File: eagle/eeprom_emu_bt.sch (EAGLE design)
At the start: 9 parts

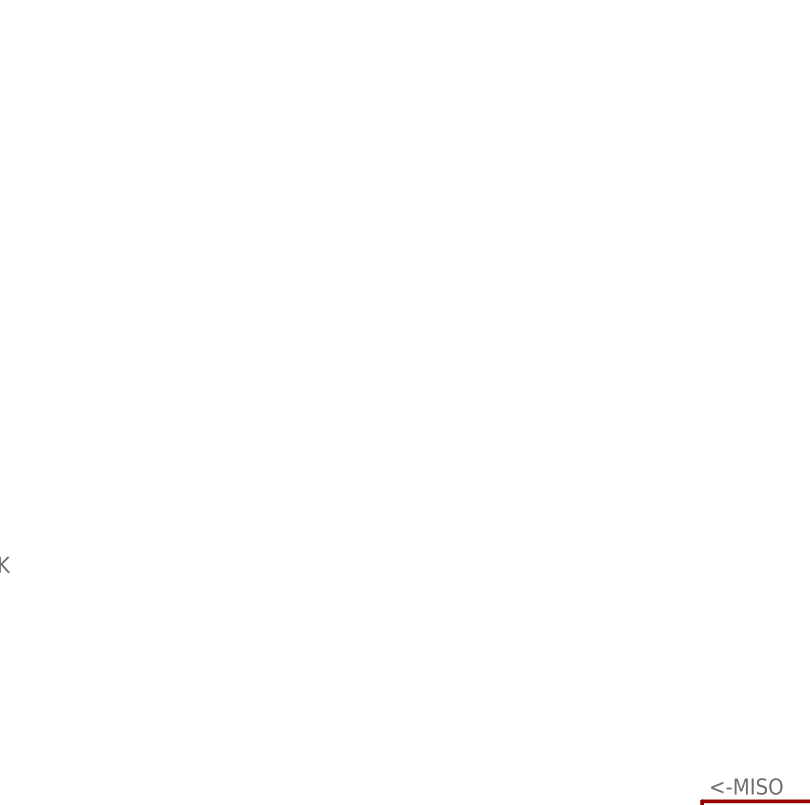
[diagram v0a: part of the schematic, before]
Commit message: 27c256 added
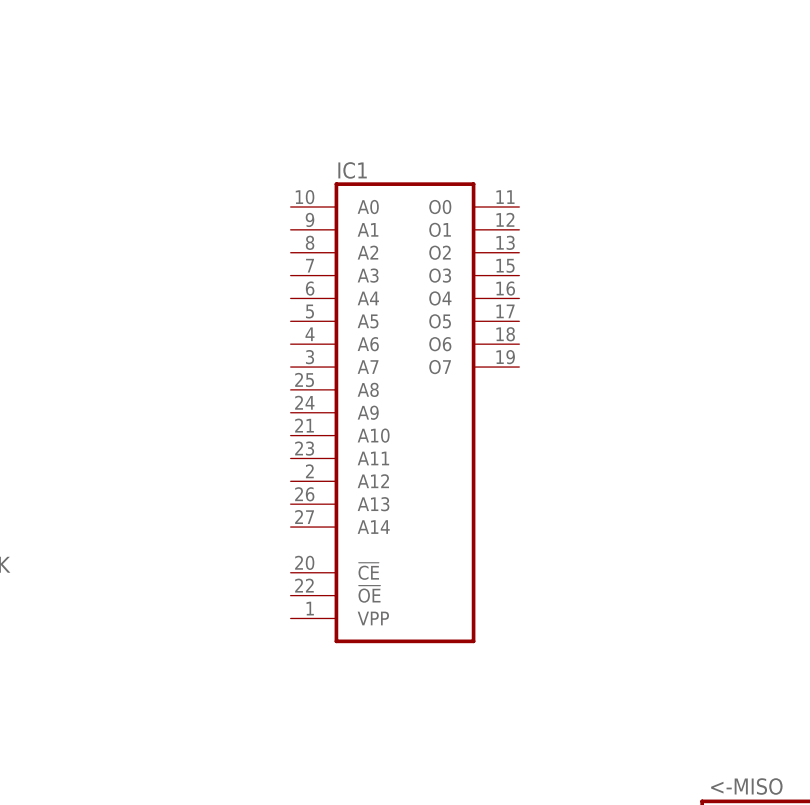
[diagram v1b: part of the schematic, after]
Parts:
- added IC1: (no value), memory:27256
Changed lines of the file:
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@@
 <part name="MAINGND18" library="supply2" deviceset="GND" device=""/>
 <part name="Y1" library="SparkFun-FreqCtrl" deviceset="CRYSTAL" device="HC49US"/>
+<part name="IC1" library="memory" deviceset="27256" device=""/>
 </parts>
 <sheets>
@@
 <instance part="MAINGND18" gate="GND" x="132.08" y="137.16"/>
 <instance part="Y1" gate="G$1" x="162.56" y="172.72" rot="R90"/>
+<instance part="IC1" gate="A" x="276.86" y="160.02"/>
 </instances>
 <busses>

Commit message: eagles
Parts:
- added BLUETOOTH: (no value), SparkFun-Connectors:M05PTH
- added IC2: IS62C256AL-45U, memory-issi-asynsram:IS62C256AL-45U
- added IC3, IC4, IC5, IC6, IC7, IC8: 74HCT541DW, 74xx-eu:74HCT541DW
- added IC9: 74HC573D, 74xx-eu:74HC573D
- added U1: SST39SF040-70-4I-NHE, Silicon_Storage_Tech_By_element14_Batch_1:SST39SF040-70-4I-NHE
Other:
- moved on the sheet: IC1
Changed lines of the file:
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@@
 <part name="Y1" library="SparkFun-FreqCtrl" deviceset="CRYSTAL" device="HC49US"/>
 <part name="IC1" library="memory" deviceset="27256" device=""/>
+<part name="U1" library="Silicon_Storage_Tech_By_element14_Batch_1" deviceset="SST39SF040-70-4I-NHE" device=""/>
+<part name="IC2" library="memory-issi-asynsram" deviceset="IS62C256AL-*" device="U" technology="45"/>
+<part name="IC3" library="74xx-eu" deviceset="74*541" device="DW" technology="HCT"/>
+<part name="IC4" library="74xx-eu" deviceset="74*541" device="DW" technology="HCT"/>
+<part name="IC5" library="74xx-eu" deviceset="74*541" device="DW" technology="HCT"/>
+<part name="IC6" library="74xx-eu" deviceset="74*541" device="DW" technology="HCT"/>
+<part name="IC7" library="74xx-eu" deviceset="74*541" device="DW" technology="HCT"/>
+<part name="IC8" library="74xx-eu" deviceset="74*541" device="DW" technology="HCT"/>
+<part name="IC9" library="74xx-eu" deviceset="74*573" device="D" technology="HC"/>
+<part name="BLUETOOTH" library="SparkFun-Connectors" deviceset="M05" device="PTH"/>
 </parts>
 <sheets>
@@
 <instance part="MAINGND18" gate="GND" x="132.08" y="137.16"/>
 <instance part="Y1" gate="G$1" x="162.56" y="172.72" rot="R90"/>
-<instance part="IC1" gate="A" x="276.86" y="160.02"/>
+<instance part="IC1" gate="A" x="307.34" y="172.72"/>
+<instance part="U1" gate="A" x="304.8" y="50.8"/>
+<instance part="IC2" gate="SRAM" x="360.68" y="175.26"/>
+<instance part="IC3" gate="A" x="419.1" y="210.82"/>
+<instance part="IC4" gate="A" x="419.1" y="170.18"/>
+<instance part="IC5" gate="A" x="419.1" y="129.54"/>
+<instance part="IC6" gate="A" x="419.1" y="78.74"/>
+<instance part="IC7" gate="A" x="419.1" y="38.1"/>
+<instance part="IC8" gate="A" x="419.1" y="0"/>
+<instance part="IC9" gate="A" x="360.68" y="124.46"/>
+<instance part="BLUETOOTH" gate="G$1" x="119.38" y="101.6"/>
 </instances>
 <busses>

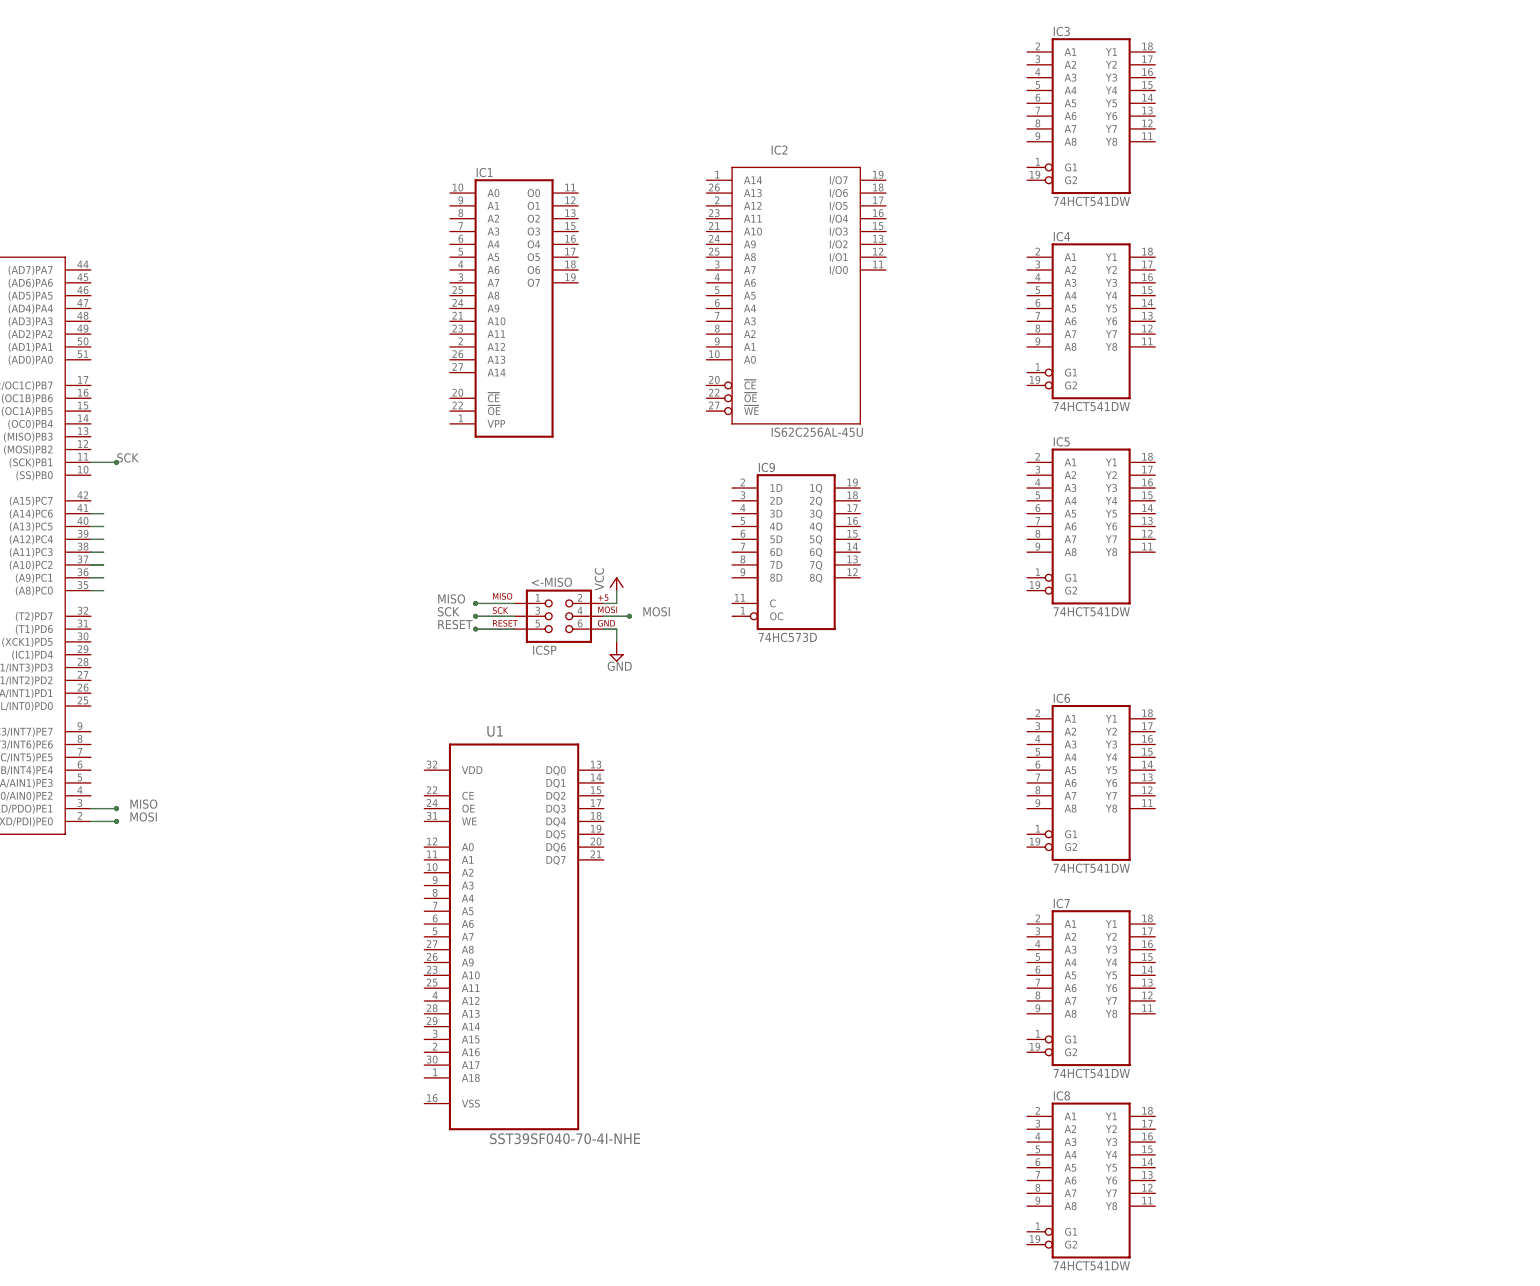
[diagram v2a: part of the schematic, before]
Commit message: or gate added for CE of sram
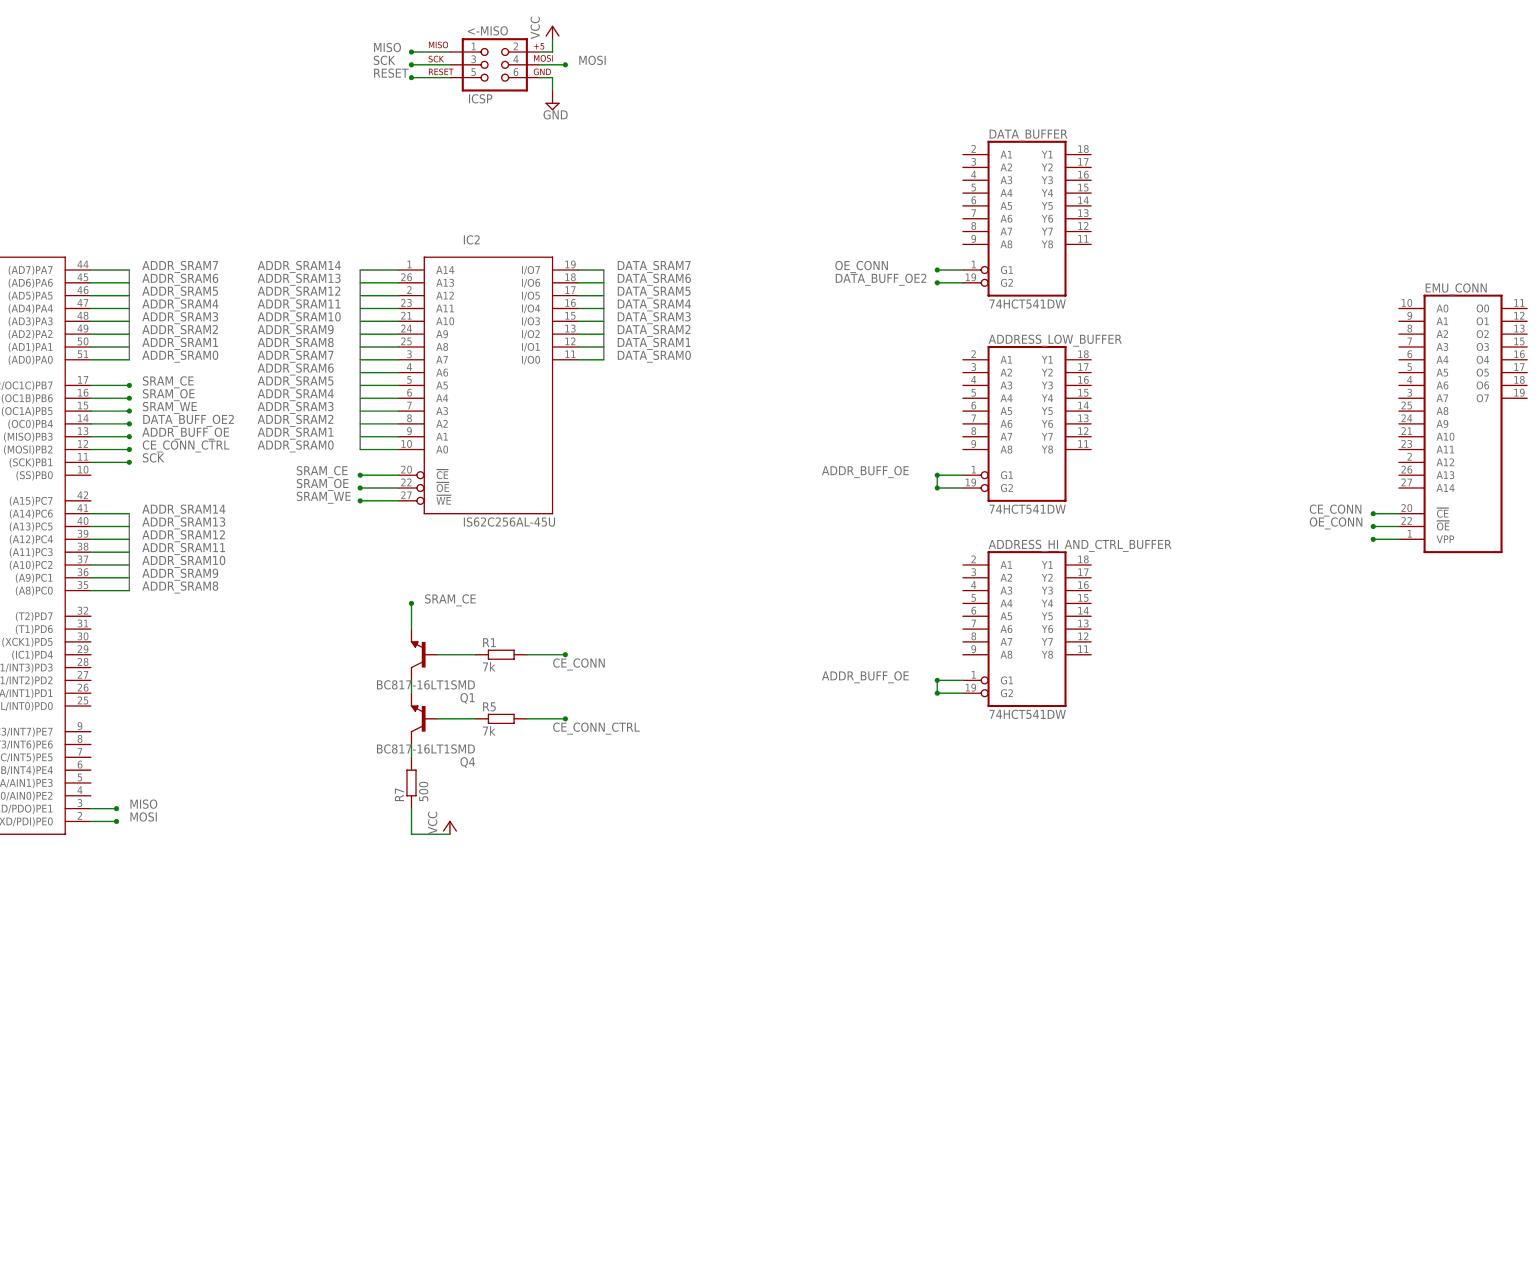
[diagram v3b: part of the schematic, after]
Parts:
- removed IC1: (no value), memory:27256
- removed IC3, IC4, IC5, IC6, IC7, IC8: 74HCT541DW, 74xx-eu:74HCT541DW
- removed IC9: 74HC573D, 74xx-eu:74HC573D
- removed U1: SST39SF040-70-4I-NHE, Silicon_Storage_Tech_By_element14_Batch_1:SST39SF040-70-4I-NHE
- added ADDRESS_HI_AND_CTRL_BUFFER, ADDRESS_LOW_BUFFER, DATA_BUFFER: 74HCT541DW, 74xx-eu:74HCT541DW
- added EMU_CONN: (no value), memory:27256
- added Q1, Q4: BC817-16LT1SMD, transistor-npn:BC817-16LT1SMD
- added R1, R5: 7k, rcl:R-EU_R0805
- added R7: 500, rcl:R-EU_R0805
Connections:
- removed net A10: ..(A10)PC2
- removed net A11: ..(A11)PC3
- removed net A12: ..(A12)PC4
- removed net A13: ..(A13)PC5
- removed net A14: ..(A14)PC6
- removed net A8: ..(A8)PC0
- removed net A9: ..(A9)PC1
- new net ADDR_BUFF_OE: ..(MISO)PB3, ADDRESS_HI_AND_CTRL_BUFFERA.G1, ADDRESS_HI_AND_CTRL_BUFFERA.G2, ADDRESS_LOW_BUFFERA.G1, ADDRESS_LOW_BUFFERA.G2
- new net ADDR_SRAM0: ..(AD0)PA0, IC2SRAM.A0
- new net ADDR_SRAM1: ..(AD1)PA1, IC2SRAM.A1
- new net ADDR_SRAM10: ..(A10)PC2, IC2SRAM.A10
- new net ADDR_SRAM11: ..(A11)PC3, IC2SRAM.A11
- new net ADDR_SRAM12: ..(A12)PC4, IC2SRAM.A12
- new net ADDR_SRAM13: ..(A13)PC5, IC2SRAM.A13
- new net ADDR_SRAM14: ..(A14)PC6, IC2SRAM.A14
- new net ADDR_SRAM2: ..(AD2)PA2, IC2SRAM.A2
- new net ADDR_SRAM3: ..(AD3)PA3, IC2SRAM.A3
- new net ADDR_SRAM4: ..(AD4)PA4, IC2SRAM.A4
- new net ADDR_SRAM5: ..(AD5)PA5, IC2SRAM.A5
- new net ADDR_SRAM6: ..(AD6)PA6, IC2SRAM.A6
- new net ADDR_SRAM7: ..(AD7)PA7, IC2SRAM.A7
- new net ADDR_SRAM8: ..(A8)PC0, IC2SRAM.A8
- new net ADDR_SRAM9: ..(A9)PC1, IC2SRAM.A9
- new net CE_CONN: EMU_CONNA.!CE, R1.2
- new net CE_CONN_CTRL: ..(MOSI)PB2, R5.2
- new net DATA_BUFF_OE2: ..(OC0)PB4, DATA_BUFFERA.G2
- new net DATA_SRAM0: IC2SRAM.I/O0
- new net DATA_SRAM1: IC2SRAM.I/O1
- new net DATA_SRAM2: IC2SRAM.I/O2
- new net DATA_SRAM3: IC2SRAM.I/O3
- new net DATA_SRAM4: IC2SRAM.I/O4
- new net DATA_SRAM5: IC2SRAM.I/O5
- new net DATA_SRAM6: IC2SRAM.I/O6
- new net DATA_SRAM7: IC2SRAM.I/O7
- new net N$3: Q1.C, Q4.E
- new net N$31: Q4.B, R5.1
- new net N$4: Q1.B, R1.1
- new net N$9: EMU_CONNA.VPP
- new net OE_CONN: DATA_BUFFERA.G1, EMU_CONNA.!OE
- new net SRAM_CE: ..(OC2/OC1C)PB7, IC2SRAM.!CE, Q1.E
- new net SRAM_OE: ..(OC1B)PB6, IC2SRAM.!OE
- new net SRAM_WE: ..(OC1A)PB5, IC2SRAM.!WE
- new net VPP: Q4.C, R7.2
- net VCC: now also R7.1
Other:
- moved on the sheet: <-MISO, IC2
